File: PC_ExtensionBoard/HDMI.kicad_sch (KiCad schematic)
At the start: 41 parts, among them J1 Conn_01x26_MountingPin, Q10 2SK3018, Q11 2N7002, Q6 2SK3018, Q9 2SK3018, U5 TPAZ1023-04F, U6 TPAZ1023-04F

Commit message: update LCSC Number
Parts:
- removed C115, C116: C_100n_0402, PC_Components_1:C_0402_1005Metric, symbol A_PC_ExtensionBoard:C_100n_0402
- added R80, R81: R_10k_0402, PC_Components_1:R_0402_1005Metric, symbol A_PC_ExtensionBoard:R_10k_0402
- C1, C2, C3, C4, C8, C9: footprint Capacitor_SMD:C_0402_1005Metric -> PC_Components_1:C_0402_1005Metric
- C19, C20: footprint A_HDJ_Library:C_0402_1005Metric -> PC_Components_1:C_0402_1005Metric
- D2, D4: footprint A_HDJ_Library:D_0402_1005Metric -> PC_Components_1:D0402-BI
- D7: footprint Diode_SMD:D_0402_1005Metric -> PC_Components_1:D0402-BI
- U5, U6: footprint A_HDJ_Library:Diodes_UDFN-10_1.0x2.5mm_P0.5mm -> PC_Components_1:DFN2510-10_L2.5-W1.0-P0.50-BL
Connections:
- net +3V3: now also R80.1, R81.1
- net GND: no longer HDMI1.SH
- new net DDI1_AUX_SEL: R80.2
- new net DDI2_AUX_SEL: R81.2

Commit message: update Schematic
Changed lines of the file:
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@@
 	)
 	(junction
-		(at 158.75 312.42)
-		(diameter 0)
-		(color 0 0 0 0)
-	)
-	(junction
 		(at 81.28 368.3)
 		(diameter 0)
@@
 	)
 	(junction
-		(at 283.21 276.86)
+		(at 273.05 276.86)
 		(diameter 0)
 		(color 0 0 0 0)
@@
 	(wire
 		(pts
-			(xy 275.59 276.86) (xy 278.13 276.86)
-		)
-		(stroke
-			(width 0)
-			(type default)
-		)
-	)
-	(wire
-		(pts
 			(xy 149.86 295.91) (xy 158.75 295.91)
 		)
@@
 	(wire
 		(pts
-			(xy 161.29 312.42) (xy 158.75 312.42)
-		)
-		(stroke
-			(width 0)
-			(type default)
-		)
-	)
-	(wire
-		(pts
 			(xy 125.73 234.95) (xy 193.04 234.95)
 		)
@@
 	(wire
 		(pts
-			(xy 137.16 346.71) (xy 123.19 346.71)
+			(xy 158.75 309.88) (xy 158.75 312.42)
 		)
 		(stroke
@@
 	(wire
 		(pts
-			(xy 111.76 143.51) (xy 76.2 143.51)
+			(xy 137.16 346.71) (xy 123.19 346.71)
 		)
 		(stroke
@@
 	(wire
 		(pts
-			(xy 139.7 175.26) (xy 139.7 180.34)
+			(xy 111.76 143.51) (xy 76.2 143.51)
 		)
 		(stroke
@@
 	(wire
 		(pts
-			(xy 273.05 276.86) (xy 275.59 276.86)
+			(xy 139.7 175.26) (xy 139.7 180.34)
 		)
 		(stroke
@@
 	(wire
 		(pts
-			(xy 273.05 271.78) (xy 273.05 276.86)
-		)
-		(stroke
-			(width 0)
-			(type default)
-		)
-	)
-	(wire
-		(pts
 			(xy 91.44 316.23) (xy 91.44 312.42)
 		)
@@
 	(wire
 		(pts
+			(xy 273.05 271.78) (xy 273.05 276.86)
+		)
+		(stroke
+			(width 0)
+			(type default)
+		)
+	)
+	(wire
+		(pts
 			(xy 132.08 290.83) (xy 132.08 289.56)
 		)
@@
 	(wire
 		(pts
-			(xy 278.13 276.86) (xy 280.67 276.86)
-		)
-		(stroke
-			(width 0)
-			(type default)
-		)
-	)
-	(wire
-		(pts
-			(xy 280.67 276.86) (xy 283.21 276.86)
+			(xy 116.84 248.92) (xy 101.6 248.92)
 		)
 		(stroke
@@
 	(wire
 		(pts
-			(xy 116.84 248.92) (xy 101.6 248.92)
+			(xy 116.84 289.56) (xy 113.03 289.56)
 		)
 		(stroke
@@
 	(wire
 		(pts
-			(xy 116.84 289.56) (xy 113.03 289.56)
+			(xy 273.05 276.86) (xy 283.21 276.86)
 		)
 		(stroke
@@
 	)
 	(symbol
+		(lib_id "power:PWR_FLAG")
+		(at 91.44 312.42 0)
+		(unit 1)
+		(body_style 1)
+		(exclude_from_sim no)
+		(in_bom yes)
+		(on_board yes)
+		(in_pos_files yes)
+		(dnp no)
+		(fields_autoplaced yes)
+		(property "Reference" "#FLG07"
+			(at 91.44 310.515 0)
+			(hide yes)
+			(show_name no)
+			(do_not_autoplace no)
+			(effects
+				(font
+					(size 1.27 1.27)
+				)
+			)
+		)
+		(property "Value" "PWR_FLAG"
+			(at 91.44 307.34 0)
+			(show_name no)
+			(do_not_autoplace no)
+			(effects
+				(font
+					(size 1.27 1.27)
+				)
+			)
+		)
+		(property "Footprint" ""
+			(at 91.44 312.42 0)
+			(hide yes)
+			(show_name no)
+			(do_not_autoplace no)
+			(effects
+				(font
+					(size 1.27 1.27)
+				)
+			)
+		)
+		(property "Datasheet" ""
+			(at 91.44 312.42 0)
+			(hide yes)
+			(show_name no)
+			(do_not_autoplace no)
+			(effects
+				(font
+					(size 1.27 1.27)
+				)
+			)
+		)
+		(property "Description" "Special symbol for telling ERC where power comes from"
+			(at 91.44 312.42 0)
+			(hide yes)
+			(show_name no)
+			(do_not_autoplace no)
+			(effects
+				(font
+					(size 1.27 1.27)
+				)
+			)
+		)
+		(pin "1"
+		)
+		(instances
+			(project "PC_ExtensionBoard"
+				(path "/6f8c8ec7-fa36-4248-8716-390866a3d0b0/6483f6bc-b70b-4928-93ba-bd87660c8c1d"
+					(reference "#FLG07")
+					(unit 1)
+				)
+			)
+		)
+	)
+	(symbol
 		(lib_id "A_PC_ExtensionBoard:1N5819WS")
 		(at 148.59 312.42 0)
@@
 	(symbol
 		(lib_id "power:GND")
-		(at 283.21 276.86 0)
+		(at 273.05 276.86 0)
 		(unit 1)
 		(body_style 1)
@@
 		(fields_autoplaced yes)
 		(property "Reference" "#PWR051"
-			(at 283.21 283.21 0)
+			(at 273.05 283.21 0)
 			(hide yes)
 			(show_name no)
@@
 		)
 		(property "Value" "GND"
-			(at 283.21 281.94 0)
+			(at 273.05 281.94 0)
 			(show_name no)
 			(do_not_autoplace no)
@@
 		)
 		(property "Footprint" ""
-			(at 283.21 276.86 0)
+			(at 273.05 276.86 0)
 			(hide yes)
 			(show_name no)
@@
 		)
 		(property "Datasheet" ""
-			(at 283.21 276.86 0)
+			(at 273.05 276.86 0)
 			(hide yes)
 			(show_name no)
@@
 		)
 		(property "Description" ""
-			(at 283.21 276.86 0)
+			(at 273.05 276.86 0)
 			(hide yes)
 			(show_name no)
@@
 	(symbol
 		(lib_id "power:+5V")
-		(at 158.75 312.42 0)
+		(at 158.75 309.88 0)
 		(unit 1)
 		(body_style 1)
@@
 		(fields_autoplaced yes)
 		(property "Reference" "#PWR043"
-			(at 158.75 316.23 0)
+			(at 158.75 313.69 0)
 			(hide yes)
 			(show_name no)
@@
 		)
 		(property "Value" "+5V"
-			(at 158.75 307.34 0)
+			(at 158.75 304.8 0)
 			(show_name no)
 			(do_not_autoplace no)
@@
 		)
 		(property "Footprint" ""
-			(at 158.75 312.42 0)
+			(at 158.75 309.88 0)
 			(hide yes)
 			(show_name no)
@@
 		)
 		(property "Datasheet" ""
-			(at 158.75 312.42 0)
+			(at 158.75 309.88 0)
 			(hide yes)
 			(show_name no)
@@
 		)
 		(property "Description" ""
-			(at 158.75 312.42 0)
+			(at 158.75 309.88 0)
 			(hide yes)
 			(show_name no)
@@
 					(unit 1)
 				)
-			)
-		)
-	)
-	(symbol
-		(lib_id "power:PWR_FLAG")
-		(at 161.29 312.42 270)
-		(unit 1)
-		(body_style 1)
-		(exclude_from_sim no)
-		(in_bom yes)
-		(on_board yes)
-		(in_pos_files yes)
-		(dnp no)
-		(fields_autoplaced yes)
-		(property "Reference" "#FLG05"
-			(at 163.195 312.42 0)
-			(hide yes)
-			(show_name no)
-			(do_not_autoplace no)
-			(effects
-				(font
-					(size 1.27 1.27)
-				)
-			)
-		)
-		(property "Value" "PWR_FLAG"
-			(at 165.1 312.4199 90)
-			(show_name no)
-			(do_not_autoplace no)
-			(effects
-				(font
-					(size 1.27 1.27)
-				)
-				(justify left)
-			)
-		)
-		(property "Footprint" ""
-			(at 161.29 312.42 0)
-			(hide yes)
-			(show_name no)
-			(do_not_autoplace no)
-			(effects
-				(font
-					(size 1.27 1.27)
-				)
-			)
-		)
-		(property "Datasheet" ""
-			(at 161.29 312.42 0)
-			(hide yes)
-			(show_name no)
-			(do_not_autoplace no)
-			(effects
-				(font
-					(size 1.27 1.27)
-				)
-			)
-		)
-		(property "Description" "Special symbol for telling ERC where power comes from"
-			(at 161.29 312.42 0)
-			(hide yes)
-			(show_name no)
-			(do_not_autoplace no)
-			(effects
-				(font
-					(size 1.27 1.27)
-				)
-			)
-		)
-		(pin "1"
-		)
-		(instances
-			(project "PC_ExtensionBoard"
-				(path "/6f8c8ec7-fa36-4248-8716-390866a3d0b0/6483f6bc-b70b-4928-93ba-bd87660c8c1d"
-					(reference "#FLG05")
-					(unit 1)
-				)

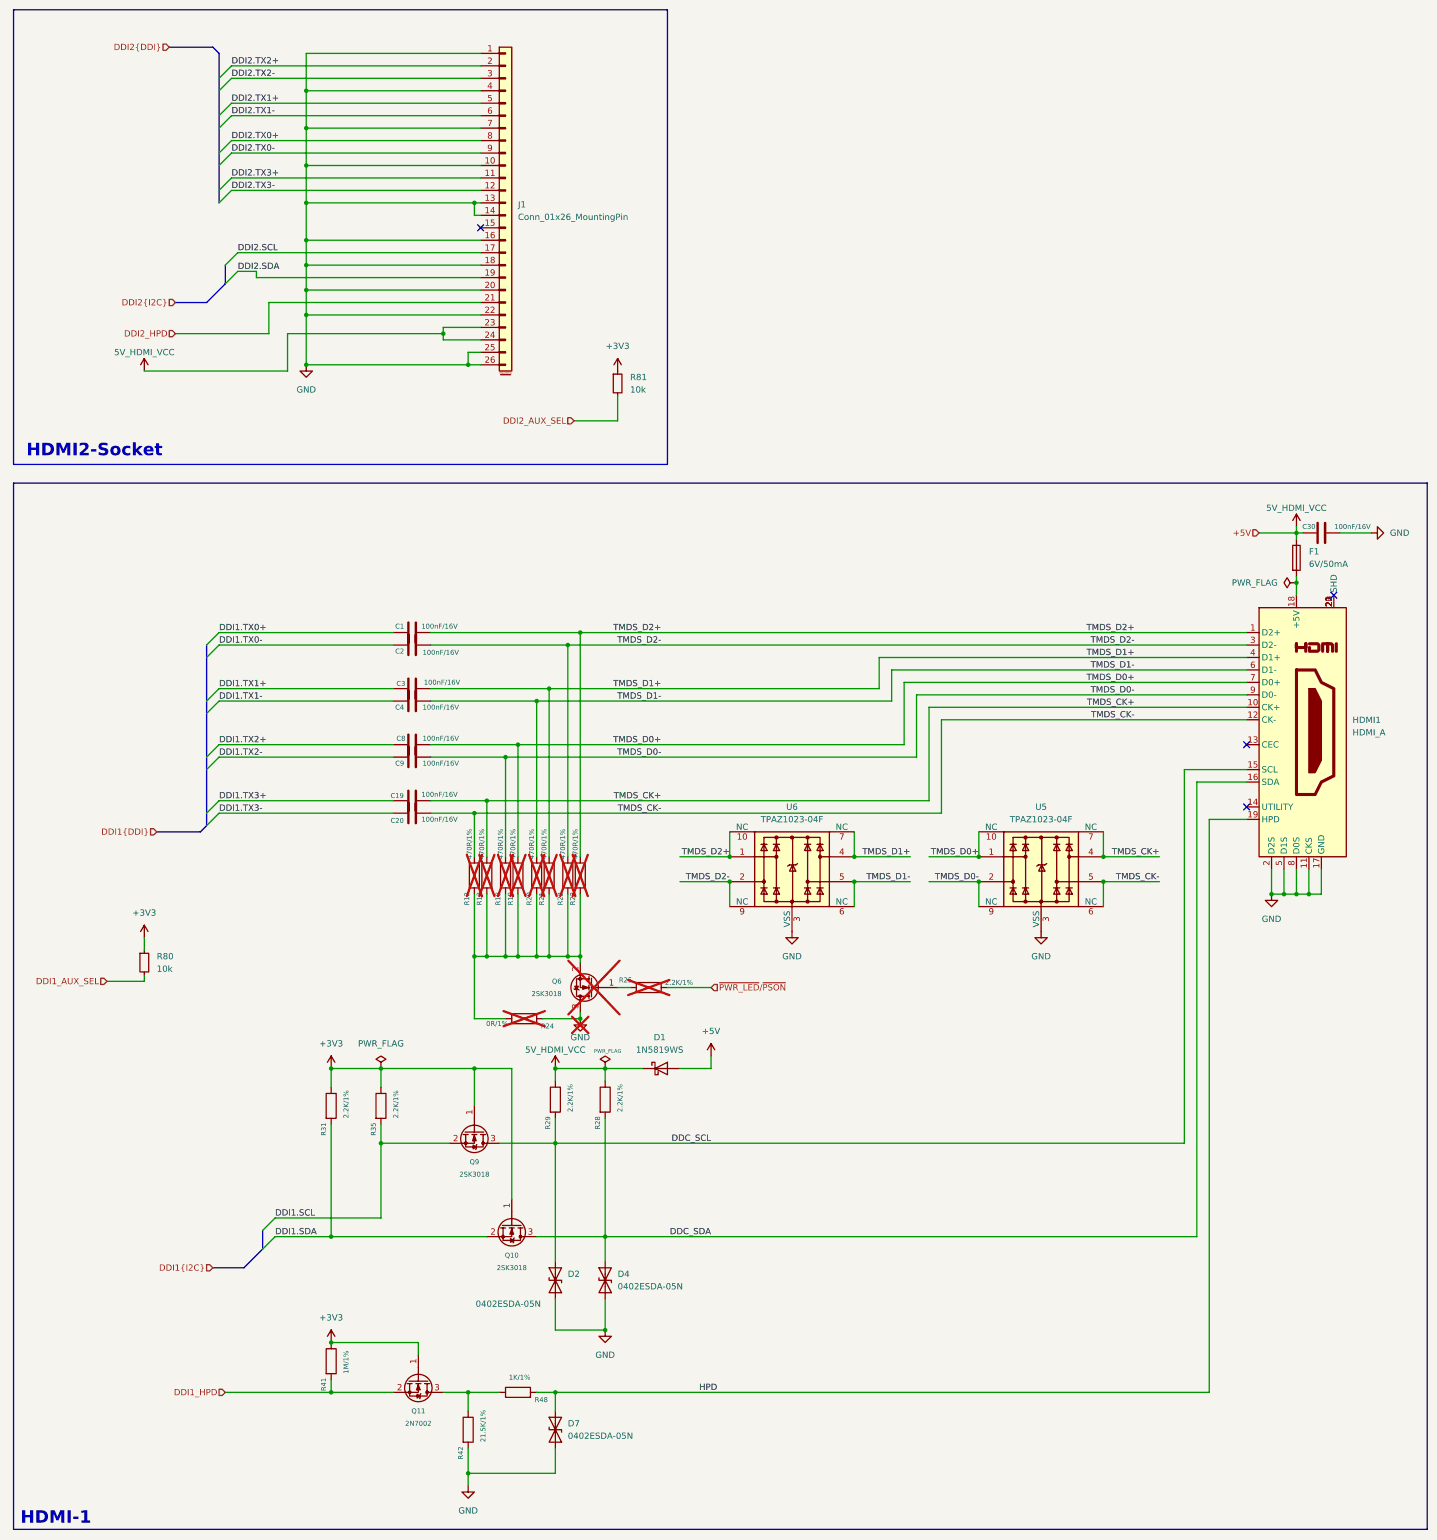
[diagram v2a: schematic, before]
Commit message: update diff pair routing
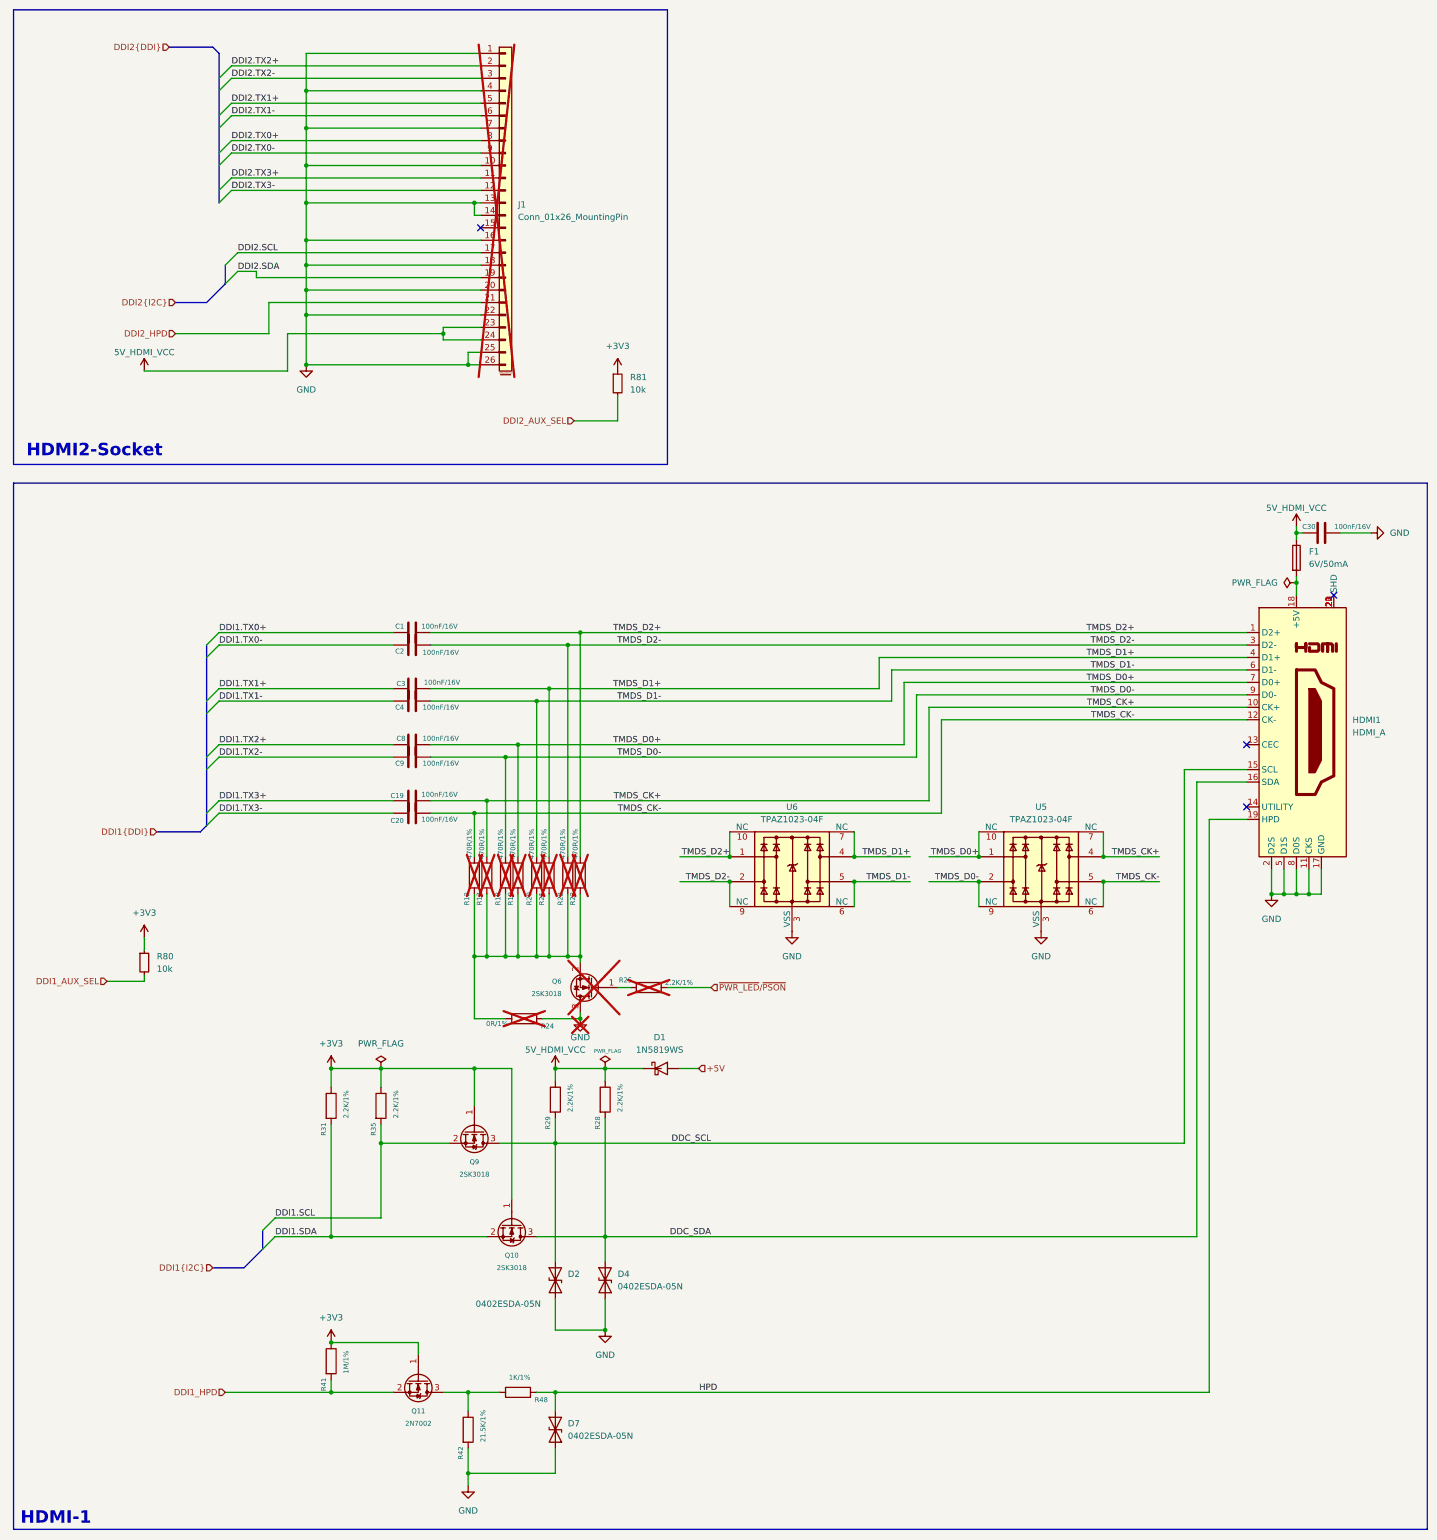
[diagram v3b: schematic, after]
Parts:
- J1: now not fitted; now left out of the parts list
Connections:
- net +5V: no longer C30.1, D1.1 (K), F1.1, J1.23 (Pin_23), J1.24 (Pin_24), R28.1, R29.1
- new net 5V_HDMI_VCC: C30.1, D1.1 (K), F1.1, J1.23 (Pin_23), J1.24 (Pin_24), R28.1, R29.1
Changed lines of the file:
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@@
 		)
 	)
-	(wire
-		(pts
-			(xy 270.51 203.2) (xy 278.13 203.2)
-		)
-		(stroke
-			(width 0)
-			(type default)
-		)
-	)
 	(bus
 		(pts
@@
 	(wire
 		(pts
-			(xy 158.75 309.88) (xy 158.75 312.42)
-		)
-		(stroke
-			(width 0)
-			(type default)
-		)
-	)
-	(wire
-		(pts
 			(xy 137.16 346.71) (xy 123.19 346.71)
 		)
@@
 	(wire
 		(pts
-			(xy 152.4 312.42) (xy 158.75 312.42)
-		)
-		(stroke
-			(width 0)
-			(type default)
-		)
-	)
-	(wire
-		(pts
 			(xy 110.49 260.35) (xy 110.49 269.24)
 		)
@@
 	(wire
 		(pts
+			(xy 156.21 312.42) (xy 152.4 312.42)
+		)
+		(stroke
+			(width 0)
+			(type default)
+		)
+	)
+	(wire
+		(pts
 			(xy 109.22 168.91) (xy 111.76 168.91)
 		)
@@
 	(hierarchical_label "+5V"
 		(shape input)
-		(at 270.51 203.2 180)
+		(at 156.21 312.42 0)
 		(effects
 			(font
 				(size 1.27 1.27)
 			)
-			(justify right)
+			(justify left)
 		)
 	)
@@
 		(body_style 1)
 		(exclude_from_sim no)
-		(in_bom yes)
-		(on_board yes)
-		(in_pos_files yes)
-		(dnp no)
+		(in_bom no)
+		(on_board no)
+		(in_pos_files no)
+		(dnp yes)
 		(fields_autoplaced yes)
 		(property "Reference" "J1"
@@
 		)
 		(property "Datasheet" "https://datasheet.lcsc.com/lcsc/2204281430_Guangdong-Hottech-1N5819WS_C191023.pdf"
-			(at 148.59 312.42 0)
+			(at 151.384 319.278 0)
 			(hide yes)
 			(show_name no)
@@
 		)
 		(property "DF_Comment" "二极管-1N5819W-SOD323备选型号:B5819WS、JSPD140A"
-			(at 148.59 312.42 0)
+			(at 151.13 317.754 0)
 			(hide yes)
 			(show_name no)
@@
 		)
 		(property "SCH_Show_Footprint" "SOD-323"
-			(at 148.59 312.42 0)
+			(at 148.844 319.024 0)
 			(hide yes)
 			(show_name no)
@@
 		)
 		(property "LCSC" "C191023"
-			(at 148.59 312.42 0)
+			(at 148.844 318.77 0)
 			(hide yes)
 			(show_name no)
@@
 					(unit 1)
 				)
-			)
-		)
-	)
-	(symbol
-		(lib_id "power:+5V")
-		(at 158.75 309.88 0)
-		(unit 1)
-		(body_style 1)
-		(exclude_from_sim no)
-		(in_bom yes)
-		(on_board yes)
-		(in_pos_files yes)
-		(dnp no)
-		(fields_autoplaced yes)
-		(property "Reference" "#PWR043"
-			(at 158.75 313.69 0)
-			(hide yes)
-			(show_name no)
-			(do_not_autoplace no)
-			(effects
-				(font
-					(size 1.27 1.27)
-				)
-			)
-		)
-		(property "Value" "+5V"
-			(at 158.75 304.8 0)
-			(show_name no)
-			(do_not_autoplace no)
-			(effects
-				(font
-					(size 1.27 1.27)
-				)
-			)
-		)
-		(property "Footprint" ""
-			(at 158.75 309.88 0)
-			(hide yes)
-			(show_name no)
-			(do_not_autoplace no)
-			(effects
-				(font
-					(size 1.27 1.27)
-				)
-			)
-		)
-		(property "Datasheet" ""
-			(at 158.75 309.88 0)
-			(hide yes)
-			(show_name no)
-			(do_not_autoplace no)
-			(effects
-				(font
-					(size 1.27 1.27)
-				)
-			)
-		)
-		(property "Description" ""
-			(at 158.75 309.88 0)
-			(hide yes)
-			(show_name no)
-			(do_not_autoplace no)
-			(effects
-				(font
-					(size 1.27 1.27)
-				)
-			)
-		)
-		(pin "1"
-		)
-		(instances
-			(project "PC_ExtensionBoard"
-				(path "/6f8c8ec7-fa36-4248-8716-390866a3d0b0/6483f6bc-b70b-4928-93ba-bd87660c8c1d"
-					(reference "#PWR043")
-					(unit 1)
-				)
